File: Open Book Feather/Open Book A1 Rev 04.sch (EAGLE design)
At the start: 127 parts, among them J1 SJ-43514-SMT, J2 10118193-0001LF, Q1 DMG341, Q2 IRLML0100, SW1 SPDT_SWITCH, U1 AP2112-3.3, U2 MCP73831T-2ACI/OT, U3 ATSAMD51J64-TQFP(10X10), U4 GD25Q16C (or GD25Q32C), U5 74AC165D, U6 GD25Q16C (or GD25Q32C), U7 MAX4468EKAT, X1 JSTPH, X2 2x5 0.05" SWD

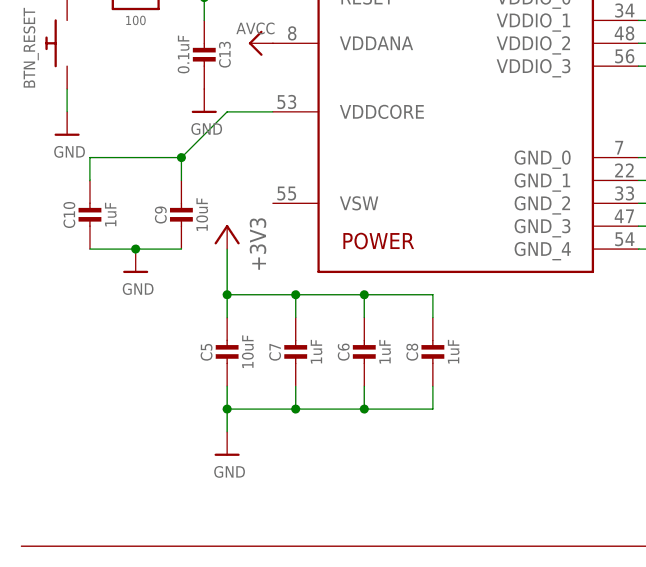
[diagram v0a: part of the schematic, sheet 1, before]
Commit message: rename capacitors around samd51
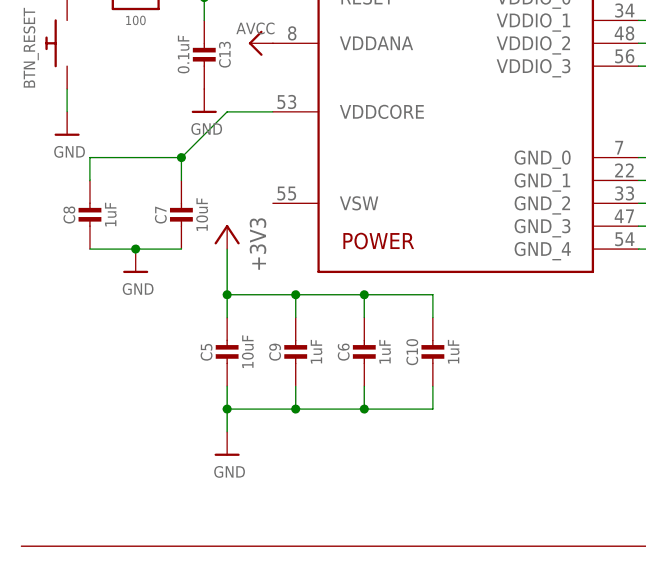
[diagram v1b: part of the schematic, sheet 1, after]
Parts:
- C7: value 1uF -> 10uF; device microbuilder:CAP_CERAMIC0805-NOOUTLINE -> microbuilder:CAP_CERAMIC0805_10MGAP
- C9: value 10uF -> 1uF; device microbuilder:CAP_CERAMIC0805_10MGAP -> microbuilder:CAP_CERAMIC0805-NOOUTLINE
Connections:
- net +3V3: now also C10.1, C9.1; no longer C7.1, C8.1
- net VDDCORE2: now also C7.1, C8.1; no longer C10.1, C9.1
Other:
- moved on the sheet: C10, C7, C8, C9
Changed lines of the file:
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@@
 <part name="+3V26" library="supply1" library_urn="urn:adsk.eagle:library:371" deviceset="+3V3" device=""/>
 <part name="U$26" library="microbuilder" deviceset="GND" device=""/>
-<part name="C9" library="microbuilder" deviceset="CAP_CERAMIC" device="0805_10MGAP" value="10uF"/>
+<part name="C7" library="microbuilder" deviceset="CAP_CERAMIC" device="0805_10MGAP" value="10uF"/>
 <part name="U$31" library="microbuilder" deviceset="GND" device=""/>
-<part name="C10" library="microbuilder" deviceset="CAP_CERAMIC" device="0805_10MGAP" value="1uF"/>
+<part name="C8" library="microbuilder" deviceset="CAP_CERAMIC" device="0805_10MGAP" value="1uF"/>
 <part name="U$32" library="microbuilder" deviceset="AVCC" device=""/>
 <part name="U$37" library="microbuilder" deviceset="AVCC" device=""/>
@@
 <part name="U$15" library="microbuilder" deviceset="GND" device=""/>
 <part name="C6" library="microbuilder" deviceset="CAP_CERAMIC" device="0805_10MGAP" value="1uF"/>
-<part name="C7" library="microbuilder" deviceset="CAP_CERAMIC" device="0805-NOOUTLINE" value="1uF"/>
+<part name="C9" library="microbuilder" deviceset="CAP_CERAMIC" device="0805-NOOUTLINE" value="1uF"/>
 <part name="U$17" library="microbuilder" deviceset="VBUS" device=""/>
 <part name="U$20" library="microbuilder" deviceset="VBAT" device=""/>
@@
 <part name="TP2" library="microbuilder" deviceset="TESTPOINT" device="ROUND2MMNO"/>
 <part name="GND7" library="supply1" deviceset="GND" device=""/>
-<part name="C8" library="microbuilder" deviceset="CAP_CERAMIC" device="0805_10MGAP" value="1uF"/>
+<part name="C10" library="microbuilder" deviceset="CAP_CERAMIC" device="0805_10MGAP" value="1uF"/>
 <part name="U$44" library="My Stuff" deviceset="OSO_GRAPHIC" device=""/>
 <part name="U$45" library="My Stuff" deviceset="OSO_BEAR" device=""/>
@@
 <attribute name="VALUE" x="382.016" y="132.08" size="1.27" layer="96"/>
 </instance>
-<instance part="C9" gate="G$1" x="327.66" y="139.7" smashed="yes">
+<instance part="C7" gate="G$1" x="327.66" y="139.7" smashed="yes">
 <attribute name="NAME" x="325.37" y="140.95" size="1.27" layer="95" font="vector" rot="R90" align="center"/>
 <attribute name="VALUE" x="329.96" y="140.95" size="1.27" layer="96" font="vector" rot="R90" align="center"/>
@@
 <attribute name="VALUE" x="321.056" y="132.08" size="1.27" layer="96"/>
 </instance>
-<instance part="C10" gate="G$1" x="317.5" y="139.7" smashed="yes">
+<instance part="C8" gate="G$1" x="317.5" y="139.7" smashed="yes">
 <attribute name="NAME" x="315.21" y="140.95" size="1.27" layer="95" font="vector" rot="R90" align="center"/>
 <attribute name="VALUE" x="319.8" y="140.95" size="1.27" layer="96" font="vector" rot="R90" align="center"/>
@@
 <attribute name="VALUE" x="350.28" y="125.71" size="1.27" layer="96" font="vector" rot="R90" align="center"/>
 </instance>
-<instance part="C7" gate="G$1" x="340.36" y="124.46" smashed="yes">
+<instance part="C9" gate="G$1" x="340.36" y="124.46" smashed="yes">
 <attribute name="NAME" x="338.07" y="125.71" size="1.27" layer="95" font="vector" rot="R90" align="center"/>
 <attribute name="VALUE" x="342.66" y="125.71" size="1.27" layer="96" font="vector" rot="R90" align="center"/>
@@
 <attribute name="VALUE" x="472.44" y="30.48" size="1.778" layer="96" align="bottom-center"/>
 </instance>
-<instance part="C8" gate="G$1" x="355.6" y="124.46" smashed="yes">
+<instance part="C10" gate="G$1" x="355.6" y="124.46" smashed="yes">
 <attribute name="NAME" x="353.31" y="125.71" size="1.27" layer="95" font="vector" rot="R90" align="center"/>
 <attribute name="VALUE" x="357.9" y="125.71" size="1.27" layer="96" font="vector" rot="R90" align="center"/>
@@
 <wire x1="317.5" y1="137.16" x2="322.58" y2="137.16" width="0.1524" layer="91"/>
 <junction x="322.58" y="137.16"/>
-<pinref part="C9" gate="G$1" pin="2"/>
+<pinref part="C7" gate="G$1" pin="2"/>
 <pinref part="U$31" gate="G$1" pin="GND"/>
-<pinref part="C10" gate="G$1" pin="2"/>
+<pinref part="C8" gate="G$1" pin="2"/>
 </segment>
 <segment>
@@
 <junction x="340.36" y="119.38"/>
 <junction x="332.74" y="119.38"/>
-<pinref part="C7" gate="G$1" pin="2"/>
-<pinref part="C8" gate="G$1" pin="2"/>
+<pinref part="C9" gate="G$1" pin="2"/>
+<pinref part="C10" gate="G$1" pin="2"/>
 <wire x1="355.6" y1="121.92" x2="355.6" y2="119.38" width="0.1524" layer="91"/>
 <wire x1="355.6" y1="119.38" x2="347.98" y2="119.38" width="0.1524" layer="91"/>
@@
 <pinref part="C6" gate="G$1" pin="1"/>
 <wire x1="347.98" y1="132.08" x2="347.98" y2="129.54" width="0.1524" layer="91"/>
-<pinref part="C7" gate="G$1" pin="1"/>
+<pinref part="C9" gate="G$1" pin="1"/>
 <wire x1="347.98" y1="132.08" x2="355.6" y2="132.08" width="0.1524" layer="91"/>
 <junction x="347.98" y="132.08"/>
-<pinref part="C8" gate="G$1" pin="1"/>
+<pinref part="C10" gate="G$1" pin="1"/>
 <wire x1="355.6" y1="132.08" x2="355.6" y2="129.54" width="0.1524" layer="91"/>
 </segment>
@@
 <junction x="327.66" y="147.32"/>
 <wire x1="332.74" y1="152.4" x2="337.82" y2="152.4" width="0.1524" layer="91"/>
-<pinref part="C9" gate="G$1" pin="1"/>
-<pinref part="C10" gate="G$1" pin="1"/>
+<pinref part="C7" gate="G$1" pin="1"/>
+<pinref part="C8" gate="G$1" pin="1"/>
 <pinref part="U3" gate="G$3" pin="VDDCORE"/>
 </segment>
